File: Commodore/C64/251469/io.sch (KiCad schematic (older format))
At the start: 24 parts, among them CN8 Control Port 2, CN9 Control Port 1, U1 6526, U2 6526, U27 74LS08, U28 4066, U8 7406

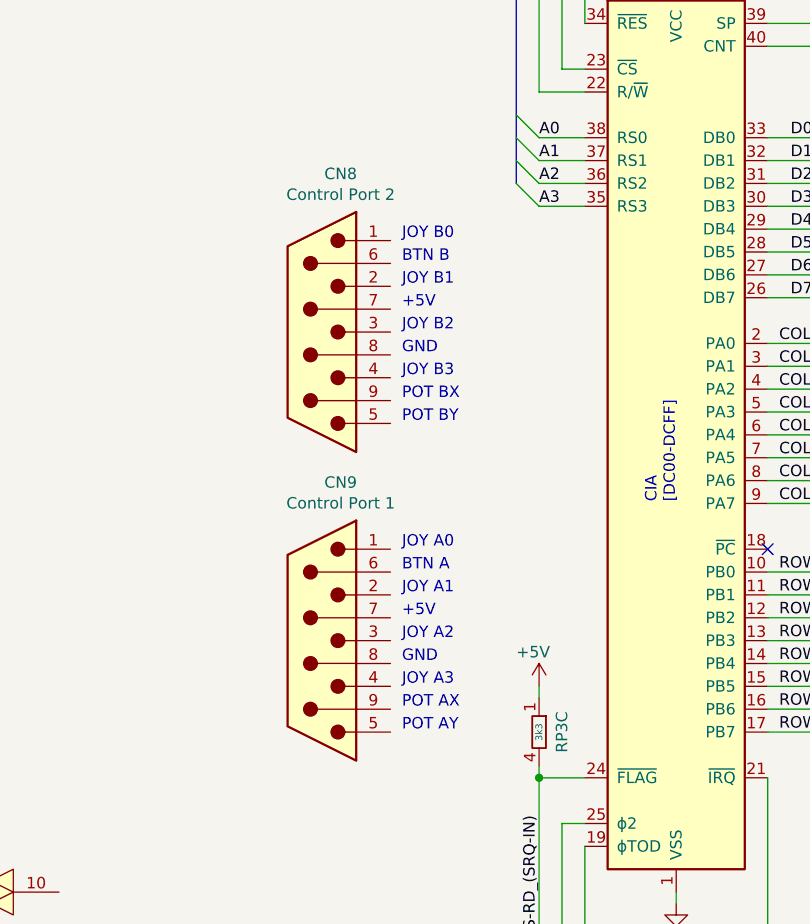
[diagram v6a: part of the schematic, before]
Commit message: Extracted control ports from general IO sheet to separate sheet
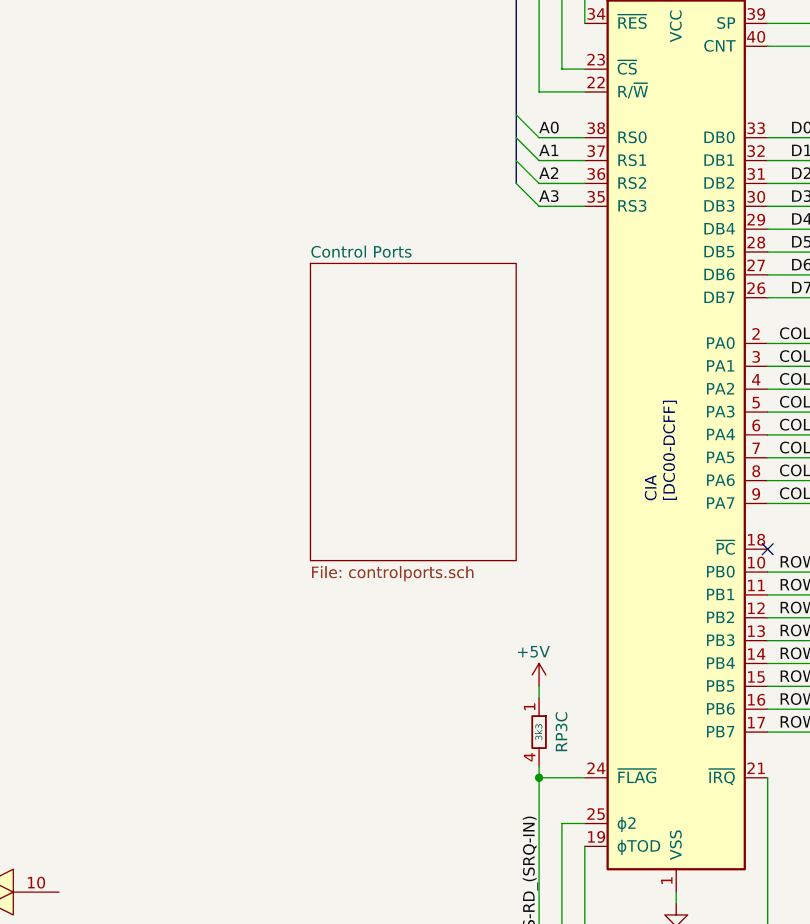
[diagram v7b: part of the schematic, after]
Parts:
- removed CN8: Control Port 2, symbol Connector:DB9_Male
- removed CN9: Control Port 1, symbol Connector:DB9_Male
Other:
- note removed: "+5V"
- note removed: "BTN A"
- note removed: "BTN B"
- note removed: "GND"
- note removed: "JOY A0"
- note removed: "JOY A1"
- note removed: "JOY A2"
- note removed: "JOY A3"
- note removed: "JOY B0"
- note removed: "JOY B1"
- note removed: "JOY B2"
- note removed: "JOY B3"
- note removed: "POT AX"
- note removed: "POT AY"
- note removed: "POT BX"
- note removed: "POT BY"
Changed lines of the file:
@@
 $Descr A4 11693 8268
 encoding utf-8
-Sheet 8 11
+Sheet 8 12
 Title "Commodore 64 - I/O Section (schematic #251469)"
 Date "2019-07-15"
@@
 UP-PA2
 $Comp
-L Connector:DB9_Male CN8
-U 1 1 5D74C9E4
-P 750 3400
-F 0 "CN8" H 668 2708 50  0000 C CNN
-F 1 "Control Port 2" H 668 2799 50  0000 C CNN
-F 2 "" H 750 3400 50  0001 C CNN
-F 3 " ~" H 750 3400 50  0001 C CNN
-	1    750  3400
-	-1   0    0    1
-$EndComp
-$Comp
-L Connector:DB9_Male CN9
-U 1 1 5D7503E1
-P 750 4750
-F 0 "CN9" H 668 4058 50  0000 C CNN
-F 1 "Control Port 1" H 668 4149 50  0000 C CNN
-F 2 "" H 750 4750 50  0001 C CNN
-F 3 " ~" H 750 4750 50  0001 C CNN
-	1    750  4750
-	-1   0    0    1
-$EndComp
-Text Notes 1100 3300 0    50   ~ 0
-+5V
-Text Notes 1100 3500 0    50   ~ 0
-GND
-Text Notes 1100 3700 0    50   ~ 0
-POT BX
-Text Notes 1100 3800 0    50   ~ 0
-POT BY
-Text Notes 1100 3000 0    50   ~ 0
-JOY B0
-Text Notes 1100 3200 0    50   ~ 0
-JOY B1
-Text Notes 1100 3400 0    50   ~ 0
-JOY B2
-Text Notes 1100 3600 0    50   ~ 0
-JOY B3
-Text Notes 1100 3100 0    50   ~ 0
-BTN B
-Text Notes 1100 4450 0    50   ~ 0
-BTN A
-Text Notes 1100 4950 0    50   ~ 0
-JOY A3
-Text Notes 1100 4750 0    50   ~ 0
-JOY A2
-Text Notes 1100 4550 0    50   ~ 0
-JOY A1
-Text Notes 1100 4350 0    50   ~ 0
-JOY A0
-Text Notes 1100 5150 0    50   ~ 0
-POT AY
-Text Notes 1100 5050 0    50   ~ 0
-POT AX
-Text Notes 1100 4850 0    50   ~ 0
-GND
-Text Notes 1100 4650 0    50   ~ 0
-+5V
-$Comp
 L 4xxx:4066 U28
 U 1 1 5D771F7B
@@
 Text Label 1700 6150 1    50   ~ 0
 CASS-RD_(SRQ-IN)
+Text Label 9000 6200 0    50   ~ 0
+TOD
+$Sheet
+S 700  3100 900  1300
+U 5D63DF34
+F0 "Control Ports" 50
+F1 "controlports.sch" 50
+$EndSheet
 Wire Bus Line
 	4500 1100 4500 2750
@@
 Wire Bus Line
 	3000 1000 3000 3150
-Text Label 9000 6200 0    50   ~ 0
-TOD
 $EndSCHEMATC

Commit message: WIP
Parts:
- removed U28: 4066, symbol 4xxx:4066
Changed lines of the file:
@@
 Text Notes 5650 3650 0    50   ~ 0
 UP-PA2
-$Comp
-L 4xxx:4066 U28
-U 1 1 5D771F7B
-P -1650 5450
-F 0 "U28" H -1650 5277 50  0000 C CNN
-F 1 "4066" H -1650 5186 50  0000 C CNN
-F 2 "" H -1650 5450 50  0001 C CNN
-F 3 "http://www.ti.com/lit/ds/symlink/cd4066b.pdf" H -1650 5450 50  0001 C CNN
-	1    -1650 5450
-	1    0    0    -1
-$EndComp
-$Comp
-L 4xxx:4066 U28
-U 2 1 5D772EE9
-P -1000 5350
-F 0 "U28" H -1000 5177 50  0000 C CNN
-F 1 "4066" H -1000 5086 50  0000 C CNN
-F 2 "" H -1000 5350 50  0001 C CNN
-F 3 "http://www.ti.com/lit/ds/symlink/cd4066b.pdf" H -1000 5350 50  0001 C CNN
-	2    -1000 5350
-	1    0    0    -1
-$EndComp
-$Comp
-L 4xxx:4066 U28
-U 3 1 5D774BE9
-P -1400 5950
-F 0 "U28" H -1400 5777 50  0000 C CNN
-F 1 "4066" H -1400 5686 50  0000 C CNN
-F 2 "" H -1400 5950 50  0001 C CNN
-F 3 "http://www.ti.com/lit/ds/symlink/cd4066b.pdf" H -1400 5950 50  0001 C CNN
-	3    -1400 5950
-	1    0    0    -1
-$EndComp
-$Comp
-L 4xxx:4066 U28
-U 4 1 5D7763E6
-P -700 5850
-F 0 "U28" H -700 5677 50  0000 C CNN
-F 1 "4066" H -700 5586 50  0000 C CNN
-F 2 "" H -700 5850 50  0001 C CNN
-F 3 "http://www.ti.com/lit/ds/symlink/cd4066b.pdf" H -700 5850 50  0001 C CNN
-	4    -700 5850
-	1    0    0    -1
-$EndComp
 Text HLabel 1100 800  0    50   BiDi ~ 0
 ~INTRST
@@
 $EndComp
 $Comp
-L power_more:9VAC1 #PWR?
+L power_more:9VAC1 #PWR0198
 U 1 1 5D3B15DC
 P 10850 5550
-F 0 "#PWR?" H 10850 5450 50  0001 C CNN
+F 0 "#PWR0198" H 10850 5450 50  0001 C CNN
 F 1 "9VAC1" H 10850 5825 50  0000 C CNN
 F 2 "" H 10850 5550 50  0001 C CNN
@@
 	10850 5900 10850 5950
 $Comp
-L power:GND #PWR?
+L power:GND #PWR0199
 U 1 1 5D3B771F
 P 10850 6300
-F 0 "#PWR?" H 10850 6050 50  0001 C CNN
+F 0 "#PWR0199" H 10850 6050 50  0001 C CNN
 F 1 "GND" H 10855 6127 50  0000 C CNN
 F 2 "" H 10850 6300 50  0001 C CNN
@@
 	10850 6250 10850 6300
 $Comp
-L power:GND #PWR?
+L power:GND #PWR0200
 U 1 1 5D3B8BE9
 P 10350 6300
-F 0 "#PWR?" H 10350 6050 50  0001 C CNN
+F 0 "#PWR0200" H 10350 6050 50  0001 C CNN
 F 1 "GND" H 10355 6127 50  0000 C CNN
 F 2 "" H 10350 6300 50  0001 C CNN
@@
 AR Path="/5D28EBAC/5D3C4989" Ref="#PWR?"  Part="1"
 AR Path="/5D4AE438/5D3C4989" Ref="#PWR?"  Part="1"
-AR Path="/5D943305/5D3C4989" Ref="#PWR?"  Part="1"
-F 0 "#PWR?" H 9900 5450 50  0001 C CNN
+AR Path="/5D943305/5D3C4989" Ref="#PWR0201"  Part="1"
+F 0 "#PWR0201" H 9900 5450 50  0001 C CNN
 F 1 "+5V" H 9800 5750 50  0000 L CNN
 F 2 "" H 9900 5600 50  0001 C CNN
@@
 F0 "Keyboard" 50
 F1 "keyboard.sch" 50
-F2 "ROW[0..7]" O L 3750 4350 50
-F3 "COL[0..7]" O L 3750 4250 50
+F2 "ROW[0..7]" B L 3750 4350 50
+F3 "COL[0..7]" B L 3750 4250 50
 F4 "NMI" O R 4450 4250 50
 $EndSheet
@@
 AR Path="/5D28EBAC/5DABFEFE" Ref="#PWR?"  Part="1"
 AR Path="/5D4AE438/5DABFEFE" Ref="#PWR?"  Part="1"
-AR Path="/5D943305/5DABFEFE" Ref="#PWR?"  Part="1"
+AR Path="/5D943305/5DABFEFE" Ref="#PWR0202"  Part="1"
 AR Path="/5D943305/5D47A471/5DABFEFE" Ref="#PWR?"  Part="1"
-F 0 "#PWR?" H 7300 2900 50  0001 C CNN
+F 0 "#PWR0202" H 7300 2900 50  0001 C CNN
 F 1 "+5V" H 7200 3200 50  0000 L CNN
 F 2 "" H 7300 3050 50  0001 C CNN
@@
 AR Path="/5D28EBAC/5D94F7F0" Ref="#PWR?"  Part="1"
 AR Path="/5D4AE438/5D94F7F0" Ref="#PWR?"  Part="1"
-AR Path="/5D943305/5D94F7F0" Ref="#PWR?"  Part="1"
+AR Path="/5D943305/5D94F7F0" Ref="#PWR0203"  Part="1"
 AR Path="/5D943305/5D47A471/5D94F7F0" Ref="#PWR?"  Part="1"
-F 0 "#PWR?" H 4100 5500 50  0001 C CNN
+F 0 "#PWR0203" H 4100 5500 50  0001 C CNN
 F 1 "+5V" H 4000 5800 50  0000 L CNN
 F 2 "" H 4100 5650 50  0001 C CNN
@@
 AR Path="/5D28EBAC/5DD390BE" Ref="#PWR?"  Part="1"
 AR Path="/5D4AE438/5DD390BE" Ref="#PWR?"  Part="1"
-AR Path="/5D943305/5DD390BE" Ref="#PWR?"  Part="1"
+AR Path="/5D943305/5DD390BE" Ref="#PWR0204"  Part="1"
 AR Path="/5D943305/5D47A471/5DD390BE" Ref="#PWR?"  Part="1"
-F 0 "#PWR?" H 7950 2900 50  0001 C CNN
+F 0 "#PWR0204" H 7950 2900 50  0001 C CNN
 F 1 "+5V" H 7850 3200 50  0000 L CNN
 F 2 "" H 7950 3050 50  0001 C CNN
@@
 AR Path="/5D28EBAC/5DE69A12" Ref="#PWR?"  Part="1"
 AR Path="/5D4AE438/5DE69A12" Ref="#PWR?"  Part="1"
-AR Path="/5D943305/5DE69A12" Ref="#PWR?"  Part="1"
+AR Path="/5D943305/5DE69A12" Ref="#PWR0205"  Part="1"
 AR Path="/5D943305/5D47A471/5DE69A12" Ref="#PWR?"  Part="1"
-F 0 "#PWR?" H 6000 7200 50  0001 C CNN
+F 0 "#PWR0205" H 6000 7200 50  0001 C CNN
 F 1 "+5V" H 5900 7500 50  0000 L CNN
 F 2 "" H 6000 7350 50  0001 C CNN
@@
 AR Path="/5D28EBAC/5DF27A3D" Ref="#PWR?"  Part="1"
 AR Path="/5D4AE438/5DF27A3D" Ref="#PWR?"  Part="1"
-AR Path="/5D943305/5DF27A3D" Ref="#PWR?"  Part="1"
+AR Path="/5D943305/5DF27A3D" Ref="#PWR0206"  Part="1"
 AR Path="/5D943305/5D47A471/5DF27A3D" Ref="#PWR?"  Part="1"
-F 0 "#PWR?" H 1700 4800 50  0001 C CNN
+F 0 "#PWR0206" H 1700 4800 50  0001 C CNN
 F 1 "+5V" H 1600 5100 50  0000 L CNN
 F 2 "" H 1700 4950 50  0001 C CNN
@@
 	8150 4800 8150 4850
 $Comp
-L power:GND #PWR?
+L power:GND #PWR0207
 U 1 1 5E000C0D
 P 8150 5200
-F 0 "#PWR?" H 8150 4950 50  0001 C CNN
+F 0 "#PWR0207" H 8150 4950 50  0001 C CNN
 F 1 "GND" H 8155 5027 50  0000 C CNN
 F 2 "" H 8150 5200 50  0001 C CNN
@@
 AR Path="/5D28EBAC/5DE2E5EA" Ref="#PWR?"  Part="1"
 AR Path="/5D4AE438/5DE2E5EA" Ref="#PWR?"  Part="1"
-AR Path="/5D943305/5DE2E5EA" Ref="#PWR?"  Part="1"
+AR Path="/5D943305/5DE2E5EA" Ref="#PWR0208"  Part="1"
 AR Path="/5D943305/5D47A471/5DE2E5EA" Ref="#PWR?"  Part="1"
-F 0 "#PWR?" H 4600 4800 50  0001 C CNN
+F 0 "#PWR0208" H 4600 4800 50  0001 C CNN
 F 1 "+5V" H 4500 5100 50  0000 L CNN
 F 2 "" H 4600 4950 50  0001 C CNN
@@
 	7750 4550 7850 4550
 $Comp
-L power:GND #PWR?
+L power:GND #PWR0209
 U 1 1 5DFF36EE
 P 7850 4600
-F 0 "#PWR?" H 7850 4350 50  0001 C CNN
+F 0 "#PWR0209" H 7850 4350 50  0001 C CNN
 F 1 "GND" H 7850 4475 50  0000 C CNN
 F 2 "" H 7850 4600 50  0001 C CNN
@@
 TOD
 $Sheet
-S 700  3100 900  1300
+S 3750 3700 800  250
 U 5D63DF34
 F0 "Control Ports" 50
 F1 "controlports.sch" 50
+F2 "ROW[0..7]" B L 3750 3850 50
+F3 "COL[0..7]" B L 3750 3750 50
 $EndSheet
 Wire Bus Line
